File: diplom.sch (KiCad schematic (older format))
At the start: 0 parts

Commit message: Sync from home
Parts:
- added C?: CP, symbol CP
- added C?: C, symbol C
- added D?: LED, symbol LED
- added DS?: WC1602A, Displays:WC1602A, symbol WC1602A
- added J?: Barrel_Jack, symbol Barrel_Jack
- added J?: Screw_Terminal_01x02, symbol Screw_Terminal_01x02
- added J?: USB_B, symbol USB_B
- added L?: L, symbol L
- added R?: R, symbol R
- added RV?: POT, symbol POT
- added Y?: Crystal, symbol Crystal
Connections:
- net labels added: +12V, +3.3V, +5V, GND
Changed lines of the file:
@@
 EESchema Schematic File Version 2
-LIBS:vladch_capacitors
-LIBS:vladch_different
-LIBS:vladch_diodes
-LIBS:vladch_resistors
 LIBS:power
 LIBS:device
@@
 Comment4 ""
 $EndDescr
+$Comp
+L +12V #PWR?
+U 1 1 5A1978B4
+P 4224 8140
+F 0 "#PWR?" H 4224 7990 50  0001 C CNN
+F 1 "+12V" H 4224 8280 50  0000 C CNN
+F 2 "" H 4224 8140 50  0001 C CNN
+F 3 "" H 4224 8140 50  0001 C CNN
+	1    4224 8140
+	1    0    0    -1
+$EndComp
+$Comp
+L +3.3V #PWR?
+U 1 1 5A1978C8
+P 4914 8104
+F 0 "#PWR?" H 4914 7954 50  0001 C CNN
+F 1 "+3.3V" H 4914 8244 50  0000 C CNN
+F 2 "" H 4914 8104 50  0001 C CNN
+F 3 "" H 4914 8104 50  0001 C CNN
+	1    4914 8104
+	1    0    0    -1
+$EndComp
+$Comp
+L +5V #PWR?
+U 1 1 5A1978DC
+P 4560 8218
+F 0 "#PWR?" H 4560 8068 50  0001 C CNN
+F 1 "+5V" H 4560 8358 50  0000 C CNN
+F 2 "" H 4560 8218 50  0001 C CNN
+F 3 "" H 4560 8218 50  0001 C CNN
+	1    4560 8218
+	1    0    0    -1
+$EndComp
+$Comp
+L GND #PWR?
+U 1 1 5A1978F0
+P 4404 8416
+F 0 "#PWR?" H 4404 8166 50  0001 C CNN
+F 1 "GND" H 4404 8266 50  0000 C CNN
+F 2 "" H 4404 8416 50  0001 C CNN
+F 3 "" H 4404 8416 50  0001 C CNN
+	1    4404 8416
+	1    0    0    -1
+$EndComp
+$Comp
+L CP C?
+U 1 1 5A197957
+P 5124 8434
+F 0 "C?" H 5149 8534 50  0000 L CNN
+F 1 "CP" H 5149 8334 50  0000 L CNN
+F 2 "" H 5162 8284 50  0001 C CNN
+F 3 "" H 5124 8434 50  0001 C CNN
+	1    5124 8434
+	1    0    0    -1
+$EndComp
+$Comp
+L C C?
+U 1 1 5A197ECB
+P 5646 8410
+F 0 "C?" H 5671 8510 50  0000 L CNN
+F 1 "C" H 5671 8310 50  0000 L CNN
+F 2 "" H 5684 8260 50  0001 C CNN
+F 3 "" H 5646 8410 50  0001 C CNN
+	1    5646 8410
+	1    0    0    -1
+$EndComp
+$Comp
+L Crystal Y?
+U 1 1 5A197FF0
+P 5556 7840
+F 0 "Y?" H 5556 7990 50  0000 C CNN
+F 1 "Crystal" H 5556 7690 50  0000 C CNN
+F 2 "" H 5556 7840 50  0001 C CNN
+F 3 "" H 5556 7840 50  0001 C CNN
+	1    5556 7840
+	1    0    0    -1
+$EndComp
+$Comp
+L L L?
+U 1 1 5A198075
+P 6150 8368
+F 0 "L?" V 6100 8368 50  0000 C CNN
+F 1 "L" V 6225 8368 50  0000 C CNN
+F 2 "" H 6150 8368 50  0001 C CNN
+F 3 "" H 6150 8368 50  0001 C CNN
+	1    6150 8368
+	1    0    0    -1
+$EndComp
+$Comp
+L LED D?
+U 1 1 5A1980F0
+P 5142 8914
+F 0 "D?" H 5142 9014 50  0000 C CNN
+F 1 "LED" H 5142 8814 50  0000 C CNN
+F 2 "" H 5142 8914 50  0001 C CNN
+F 3 "" H 5142 8914 50  0001 C CNN
+	1    5142 8914
+	1    0    0    -1
+$EndComp
+$Comp
+L POT RV?
+U 1 1 5A19818D
+P 3222 8770
+F 0 "RV?" V 3047 8770 50  0000 C CNN
+F 1 "POT" V 3122 8770 50  0000 C CNN
+F 2 "" H 3222 8770 50  0001 C CNN
+F 3 "" H 3222 8770 50  0001 C CNN
+	1    3222 8770
+	1    0    0    -1
+$EndComp
+$Comp
+L R R?
+U 1 1 5A198232
+P 4044 8992
+F 0 "R?" V 4124 8992 50  0000 C CNN
+F 1 "R" V 4044 8992 50  0000 C CNN
+F 2 "" V 3974 8992 50  0001 C CNN
+F 3 "" H 4044 8992 50  0001 C CNN
+	1    4044 8992
+	1    0    0    -1
+$EndComp
+$Comp
+L Barrel_Jack J?
+U 1 1 5A19836B
+P 6198 9490
+F 0 "J?" H 6198 9700 50  0000 C CNN
+F 1 "Barrel_Jack" H 6198 9315 50  0000 C CNN
+F 2 "" H 6248 9450 50  0001 C CNN
+F 3 "" H 6248 9450 50  0001 C CNN
+	1    6198 9490
+	1    0    0    -1
+$EndComp
+$Comp
+L Screw_Terminal_01x02 J?
+U 1 1 5A1983D6
+P 7182 8530
+F 0 "J?" H 7182 8630 50  0000 C CNN
+F 1 "Screw_Terminal_01x02" H 7182 8330 50  0000 C CNN
+F 2 "" H 7182 8530 50  0001 C CNN
+F 3 "" H 7182 8530 50  0001 C CNN
+	1    7182 8530
+	1    0    0    -1
+$EndComp
+$Comp
+L USB_B J?
+U 1 1 5A19841B
+P 6924 7588
+F 0 "J?" H 6724 8038 50  0000 L CNN
+F 1 "USB_B" H 6724 7938 50  0000 L CNN
+F 2 "" H 7074 7538 50  0001 C CNN
+F 3 "" H 7074 7538 50  0001 C CNN
+	1    6924 7588
+	1    0    0    -1
+$EndComp
+$Comp
+L WC1602A DS?
+U 1 1 5A1984E5
+P 8154 9532
+F 0 "DS?" H 7924 10282 50  0000 C CNN
+F 1 "WC1602A" H 8364 10282 50  0000 C CNN
+F 2 "Displays:WC1602A" H 8154 8632 50  0001 C CIN
+F 3 "" H 8854 9532 50  0001 C CNN
+	1    8154 9532
+	1    0    0    -1
+$EndComp
 $EndSCHEMATC

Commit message: Power added
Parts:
- removed J?: Barrel_Jack, symbol Barrel_Jack
- added C?: 0.01u, Capacitors_SMD:C_0603_HandSoldering, symbol C
- added C?: 8200p, Capacitors_SMD:C_0603_HandSoldering, symbol C
- added C?: 4.7u, Capacitors_SMD:C_0805_HandSoldering, symbol C
- added C? (x2): 10u, Capacitors_SMD:C_0805_HandSoldering, symbol C
- added C?: 47u, Capacitors_SMD:C_0805_HandSoldering, symbol C
- added C?: 0.1u, Capacitors_SMD:C_0603_HandSoldering, symbol C
- added C?: 100n, Capacitors_SMD:C_0603_HandSoldering, symbol C
- added D?: D, Diodes_SMD:D_2114, symbol D
- added J?: Barrel_Jack, Connectors:BARREL_JACK, symbol Barrel_Jack
- added L?: 3.3u, Inductors_NEOSID:Neosid_Inductor_Ms95, symbol L
- added Q?: S8050, TO-92, symbol S8050
- added R?: 1K69, Resistors_SMD:R_0603_HandSoldering, symbol R
- added R?: 100K, Resistors_SMD:R_0603_HandSoldering, symbol R
- added R?: 52K5, Resistors_SMD:R_0603_HandSoldering, symbol R
- added R? (x5): 10K, Resistors_SMD:R_0603_HandSoldering, symbol R
- added SW? (x4): SW_Push, Buttons_Switches_SMD:SW_SPST_B3U-1000P, symbol SW_Push
- added SW?: SW_SPST, Pin_Headers:Pin_Header_Straight_2x01_Pitch2.54mm, symbol SW_SPST
- added U?: PCF8574, symbol PCF8574
- added U?: LD3985M33R, SOT-23-5, symbol LD3985M33R
- added U?: TPS54620, symbol TPS54620
- added U?: TPS76833, SMD_Packages:SOIC-8-N, symbol TPS76833
- C?: value CP -> 330u; footprint (none) -> Capacitors_SMD:CP_Elec_10x10
- J?: symbol USB_B -> USB_B-RESCUE-diplom
- RV?: value POT -> 10K; footprint (none) -> Potentiometers:Potentiometer_Trimmer_ACP_CA14VSMD_Horizontal_Px13.0mm_Py10.0mm_MountLS
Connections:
- net labels added: BTN1, BTN2, BTN3, N_RST
- wire segments 0 -> 116
- no-connect marks 0 -> 4
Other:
- moved on the sheet: C?, D?, DS?, L?, R?, RV?, Y?

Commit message: Electric schema added
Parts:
- removed C?: C, symbol C
- removed D?: LED, symbol LED
- removed L?: L, symbol L
- removed R?: R, symbol R
- removed Y?: Crystal, symbol Crystal
- added C? (x3): 0.1u, Capacitors_SMD:C_0603_HandSoldering, symbol C
- added C? (x23): 100n, Capacitors_SMD:C_0603_HandSoldering, symbol C
- added C? (x3): 1u, Capacitors_SMD:C_0805_HandSoldering, symbol C
- added C? (x4): 15p, Capacitors_SMD:C_0603_HandSoldering, symbol C
- added C?: 100n, Capacitors_THT:C_Axial_L12.0mm_D6.5mm_P20.00mm_Horizontal, symbol C
- added C?: 10n, Capacitors_SMD:C_0603_HandSoldering, symbol C
- added C? (x4): 20p, Capacitors_SMD:C_0603_HandSoldering, symbol C
- added C?: 4.7u, Capacitors_SMD:C_0805_HandSoldering, symbol C
- added C?: 1u, Capacitors_SMD:CP_Elec_10x10, symbol CP
- added D? (x3): LED, Diodes_SMD:D_0805, symbol LED
- added D? (x4): D, Diodes_SMD:D_2114, symbol D
- added J? (x2): Screw_Terminal_01x04, Pin_Headers:Pin_Header_Straight_1x04_Pitch2.54mm, symbol Screw_Terminal_01x04
- added J?: USB_B, Connectors_USB:USB_Micro-B_Molex_47346-0001, symbol USB_B-RESCUE-diplom
- added J? (x2): Screw_Terminal_01x03, Pin_Headers:Pin_Header_Straight_1x03_Pitch2.54mm, symbol Screw_Terminal_01x03
- added L?: 3.3u, Inductors_NEOSID:Neosid_Inductor_Ms95, symbol L
- added R?: 100, Resistors_SMD:R_0603_HandSoldering, symbol R
- added R? (x7): 4K7, Resistors_SMD:R_0603_HandSoldering, symbol R
- added R? (x3): 2K2, Resistors_SMD:R_0603_HandSoldering, symbol R
- added R? (x2): 100M, Resistors_SMD:R_0603_HandSoldering, symbol R
- added R?: 1K5, Resistors_SMD:R_0603_HandSoldering, symbol R
- added R? (x4): 100K, Resistors_SMD:R_0603_HandSoldering, symbol R
- added SW?: SW_Push, Buttons_Switches_SMD:SW_SPST_B3U-1000P, symbol SW_Push
- added SW? (x2): SW_SPDT, Pin_Headers:Pin_Header_Straight_1x03_Pitch2.54mm, symbol SW_SPDT
- added U?: TCA9517, SMD_Packages:SOIC-8-N, symbol TCA9517
- added U?: CP2102, Housings_DFN_QFN:QFN-28-1EP_4x4mm_Pitch0.4mm, symbol CP2102
- added U? (x2): LS7366R, Housings_SOIC:SOIC-14_3.9x8.7mm_Pitch1.27mm, symbol LS7366R
- added U?: L298, Housings_SOIC:HSOP-20-1EP_11.0x15.9mm_Pitch1.27mm_SlugDown_ThermalVias, symbol L298
- added U?: STM32F103_STLINK, Housings_QFP:LQFP-48_7x7mm_Pitch0.5mm, symbol STM32F103_STLINK
- added U?: STM32F103_DC, Housings_QFP:LQFP-48_7x7mm_Pitch0.5mm, symbol STM32F103_DC
- added U?: STM32F446, symbol STM32F446
- added Y? (x4): Crystal, Crystals:Crystal_HC52-8mm_Vertical, symbol Crystal
- J?: footprint (none) -> Pin_Headers:Pin_Header_Straight_1x02_Pitch2.54mm
- J?: footprint (none) -> Connectors_USB:USB_Micro-B_Molex_47346-0001
- SW?: symbol SW_SPST -> SW_SPST-RESCUE-diplom
- U?: footprint (none) -> SMD_Packages:SO-16-L
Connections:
- net labels added: +3V3, A, B, DISP_SCL, DISP_SDA, MISO, MOSI, OE1_FLAG, OE1_MISO, OE1_MOSI, OE1_SCK, OE1_SS, OE2_FLAG, OE2_MISO, OE2_MOSI, OE2_SCK, OE2_SS, PWM, SCK, SS, STM_RX, STM_TX, SWD1_CLK, SWD1_IO, SWD2_CLK, SWD2_IO
- wire segments 116 -> 558
- no-connect marks 4 -> 16
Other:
- moved on the sheet: C?, D?, DS?, J?, L?, Q?, R?, RV?, SW?, U?

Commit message: TPS54620 footprint added. Annotations
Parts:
- removed J?: Screw_Terminal_01x03, Pin_Headers:Pin_Header_Straight_1x03_Pitch2.54mm, symbol Screw_Terminal_01x03
- added J5: Screw_Terminal_01x04, Pin_Headers:Pin_Header_Straight_1x04_Pitch2.54mm, symbol Screw_Terminal_01x04
- added R27: 470, Resistors_SMD:R_0603_HandSoldering, symbol R
- added R28: 2K2, Resistors_SMD:R_0603_HandSoldering, symbol R
- C37: renamed from C?; footprint Capacitors_SMD:CP_Elec_10x10 -> Capacitors_SMD:C_1210_HandSoldering
- L2: renamed from L?; footprint Inductors_NEOSID:Neosid_Inductor_Ms95 -> Inductors_SMD:L_0603_HandSoldering
- U3: renamed from U?; footprint (none) -> Footprints:TPS54620_PVQFN-N14
- U7: renamed from U?; footprint (none) -> Housings_QFP:LQFP-64_10x10mm_Pitch0.5mm
- gave numbers to parts that had none: 116
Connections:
- wire segments 558 -> 563

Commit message: Schematic changed
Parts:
- removed C48, C50: 15p, Capacitors_SMD:C_0603_HandSoldering, symbol C
- removed J7: Screw_Terminal_01x04, Pin_Headers:Pin_Header_Straight_1x04_Pitch2.54mm, symbol Screw_Terminal_01x04
- removed R24: 100M, Resistors_SMD:R_0603_HandSoldering, symbol R
- removed U12: LS7366R, Housings_SOIC:SOIC-14_3.9x8.7mm_Pitch1.27mm, symbol LS7366R
- removed Y4: Crystal, Crystals:Crystal_HC52-8mm_Vertical, symbol Crystal
- added C45: 470u, Capacitors_SMD:CP_Elec_10x10, symbol CP
- added C? (x2): 15p, Capacitors_SMD:C_0603_HandSoldering, symbol C
- added J?: Screw_Terminal_01x04, Pin_Headers:Pin_Header_Straight_1x04_Pitch2.54mm, symbol Screw_Terminal_01x04
- added R?: 100M, Resistors_SMD:R_0603_HandSoldering, symbol R
- added U?: LS7366R, Housings_SOIC:SOIC-14_3.9x8.7mm_Pitch1.27mm, symbol LS7366R
- added Y?: 20MHz, Crystals:Crystal_SMD_HC49-SD_HandSoldering, symbol Crystal
- C16, C2, C34: footprint Capacitors_SMD:C_0805_HandSoldering -> Capacitors_SMD:C_1206_HandSoldering
- C44: value 100n -> 0.1u
- C46: renamed from C45; footprint Capacitors_SMD:C_0603_HandSoldering -> Capacitors_SMD:C_0805_HandSoldering
- C47: renamed from C46; value 100n -> 0.1u; footprint Capacitors_THT:C_Axial_L12.0mm_D6.5mm_P20.00mm_Horizontal -> Capacitors_SMD:C_0805_HandSoldering
- D2, D5, D6, D7, D8: footprint Diodes_SMD:D_2114 -> Diodes_SMD:D_SMA_Handsoldering
- L1: footprint Inductors_NEOSID:Neosid_Inductor_Ms95 -> Inductors_SMD:L_10.4x10.4_H4.8
- L2: value 3.3u -> 600
- R27: renamed from R25; footprint Resistors_SMD:R_0603_HandSoldering -> Capacitors_SMD:C_1210_HandSoldering
- SW2: footprint Pin_Headers:Pin_Header_Straight_2x01_Pitch2.54mm -> Pin_Headers:Pin_Header_Straight_1x03_Pitch2.54mm
- Y1, Y2: value Crystal -> 8MHz; footprint Crystals:Crystal_HC52-8mm_Vertical -> Crystals:Crystal_SMD_HC49-SD_HandSoldering
- Y3: value Crystal -> 20MHz; footprint Crystals:Crystal_HC52-8mm_Vertical -> Crystals:Crystal_SMD_HC49-SD_HandSoldering
- renumbered C47 to C48, C49 to C50, R27 to R21, R28 to R22, R21 to R23, R22 to R24, R23 to R25, R26 to R28
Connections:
- wire segments 563 -> 519
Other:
- moved on the sheet: C15, C18, C20, C24, C25, C26, C28, C30, C32, C35, C36, C37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

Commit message: Elements reannotated
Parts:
- gave numbers to parts that had none: 6
- renumbered C16 to C15, C17 to C16, C19 to C17, C21 to C18, C15 to C19, C22 to C20, C18 to C21, C23 to C22, C24 to C23, C20 to C24, C36 to C35, C35 to C36, C38 to C37, C37 to C38, C46 to C45, C45 to C46, C48 to C50, C50 to C51, D2 to D1, D3 to D2, D1 to D3, J3 to J2, J2 to J3, J6 to J7, R25 to R26, R6 to R5, R7 to R6, R9 to R7, R5 to R9, U11 to U12, Y3 to Y4

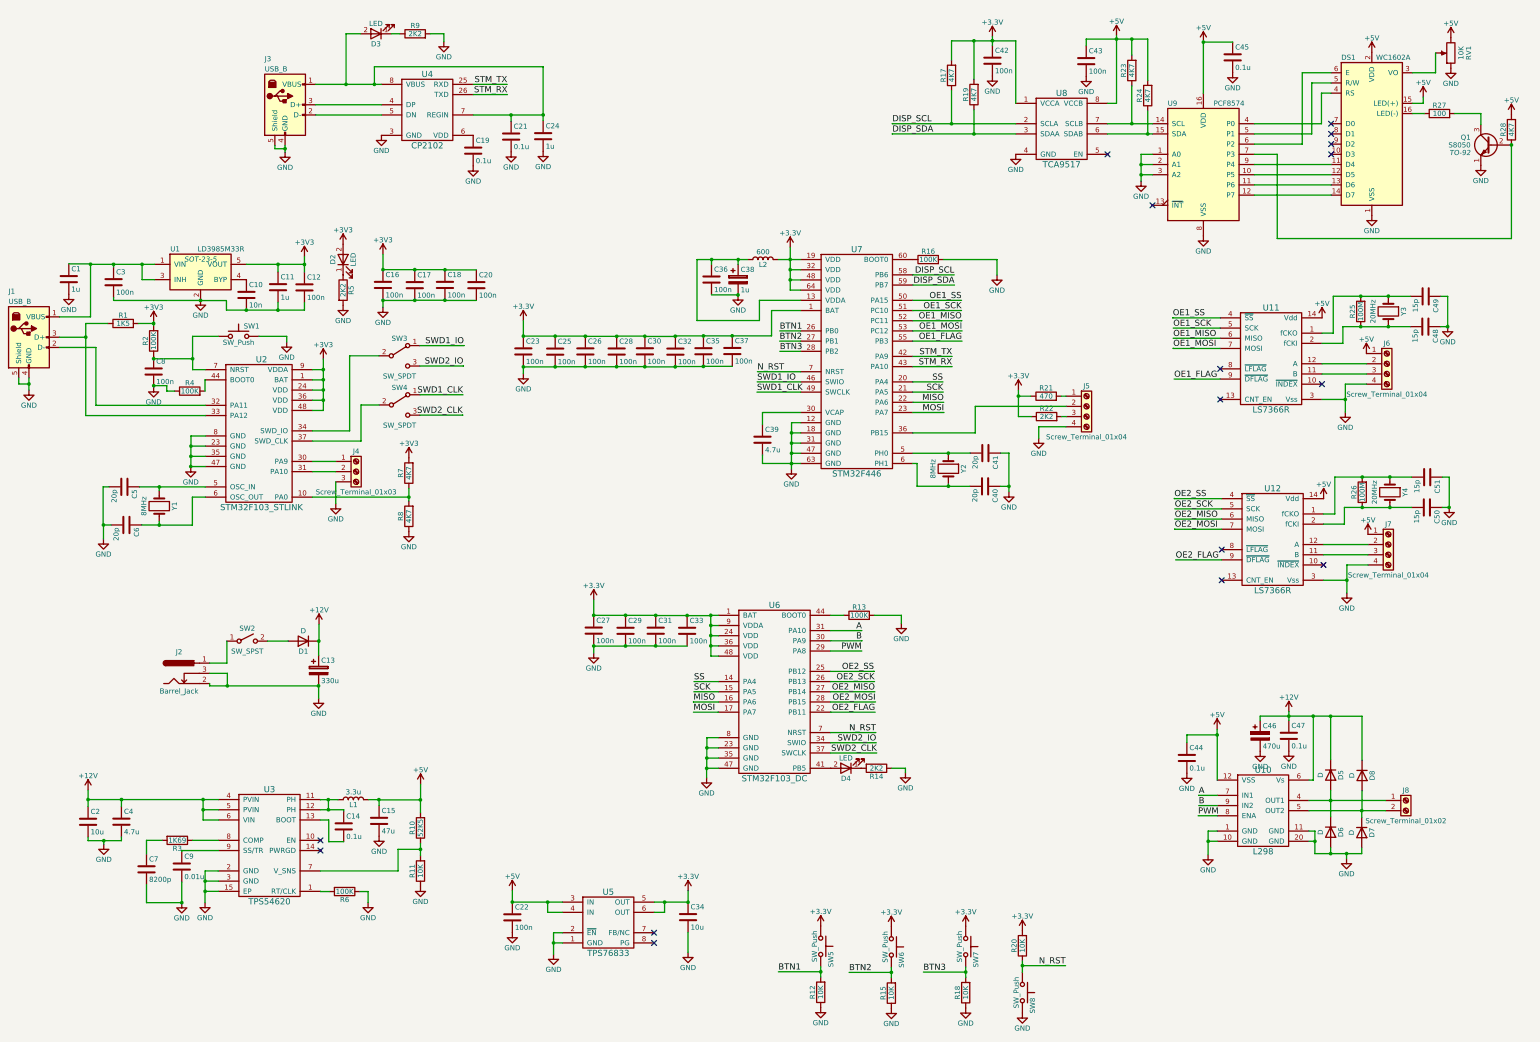
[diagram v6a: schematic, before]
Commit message: Footprints placed on PCB
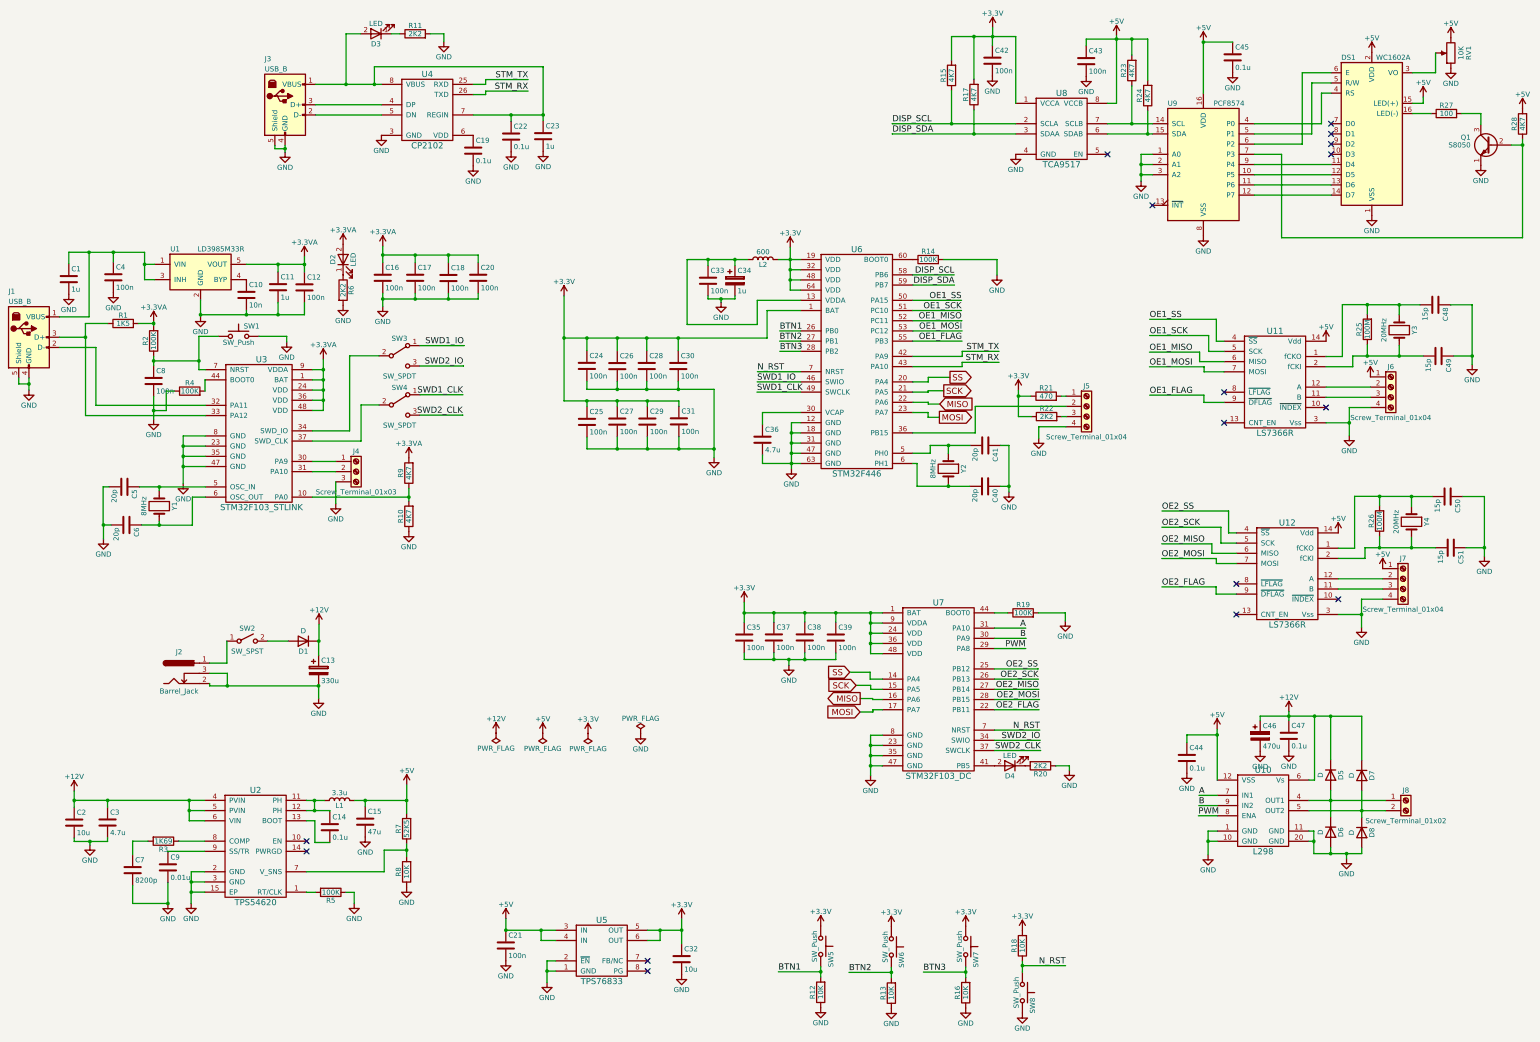
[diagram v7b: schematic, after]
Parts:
- removed R10: 52K5, Resistors_SMD:R_0603_HandSoldering, symbol R
- added R7: 52K5, Resistors_SMD:R_0603_HandSoldering, symbol R
- Q1: footprint TO-92 -> TO_SOT_Packages_THT:TO-92_Inline_Narrow_Oval
- R27: footprint Capacitors_SMD:C_1210_HandSoldering -> Resistors_SMD:R_0603_HandSoldering
- U1: footprint SOT-23-5 -> TO_SOT_Packages_SMD:SOT-23-5_HandSoldering
- renumbered C22 to C21, C21 to C22, C24 to C23, C23 to C24, C30 to C25, C25 to C26, C32 to C27, C26 to C28, C35 to C29, C4 to C3, C28 to C30, C37 to C31, C34 to C32, C36 to C33, C38 to C34, C27 to C35, C39 to C36, C29 to C37, C31 to C38, C33 to C39, C3 to C4, C51 to C50, C50 to C51, D8 to D7, D7 to D8, R8 to R10, R9 to R11, R15 to R13, R16 to R14, R17 to R15, R18 to R16, R19 to R17, R20 to R18, R13 to R19, R14 to R20, R6 to R5, R5 to R6, R11 to R8, R7 to R9, U3 to U2, U2 to U3, U7 to U6, U6 to U7
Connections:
- net labels added: +3.3VA
- net labels removed: +3V3
- wire segments 519 -> 526
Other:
- moved on the sheet: C14, C15, C16, C17, C18, C2, C20, C21, C24, C25, C26, C27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
